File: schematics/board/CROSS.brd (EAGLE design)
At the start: 82 x 82 mm, 8 parts

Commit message: Папка с платами
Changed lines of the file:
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@@
 <setting verticaltext="up"/>
 </settings>
-<grid distance="0.5" unitdist="mm" unit="mm" style="lines" multiple="1" display="yes" altdistance="0.1" altunitdist="mm" altunit="mm"/>
+<grid distance="1" unitdist="mm" unit="mm" style="lines" multiple="1" display="no" altdistance="0.01" altunitdist="mm" altunit="mm"/>
 <layers>
 <layer number="1" name="Top" color="4" fill="1" visible="yes" active="yes"/>
@@
 <layer number="43" name="vRestrict" color="2" fill="10" visible="no" active="yes"/>
 <layer number="44" name="Drills" color="7" fill="1" visible="no" active="yes"/>
-<layer number="45" name="Holes" color="7" fill="1" visible="no" active="yes"/>
+<layer number="45" name="Holes" color="7" fill="1" visible="yes" active="yes"/>
 <layer number="46" name="Milling" color="3" fill="1" visible="no" active="yes"/>
 <layer number="47" name="Measures" color="7" fill="1" visible="no" active="yes"/>
@@
 <wire x1="34.26748125" y1="24.306490625" x2="28.8618" y2="23.204940625" width="0.1" layer="20" curve="66.964296"/>
 <wire x1="23.205" y1="28.862" x2="24.306490625" y2="34.26748125" width="0.1" layer="20" curve="66.964381"/>
-<hole x="4" y="4" drill="6"/>
-<hole x="78" y="78" drill="6"/>
-<hole x="4" y="78" drill="6"/>
-<hole x="78" y="4" drill="6"/>
+<hole x="4" y="4" drill="3.5"/>
+<hole x="78" y="78" drill="3.5"/>
+<hole x="4" y="78" drill="3.5"/>
+<hole x="78" y="4" drill="3.5"/>
 </plain>
 <attributes>

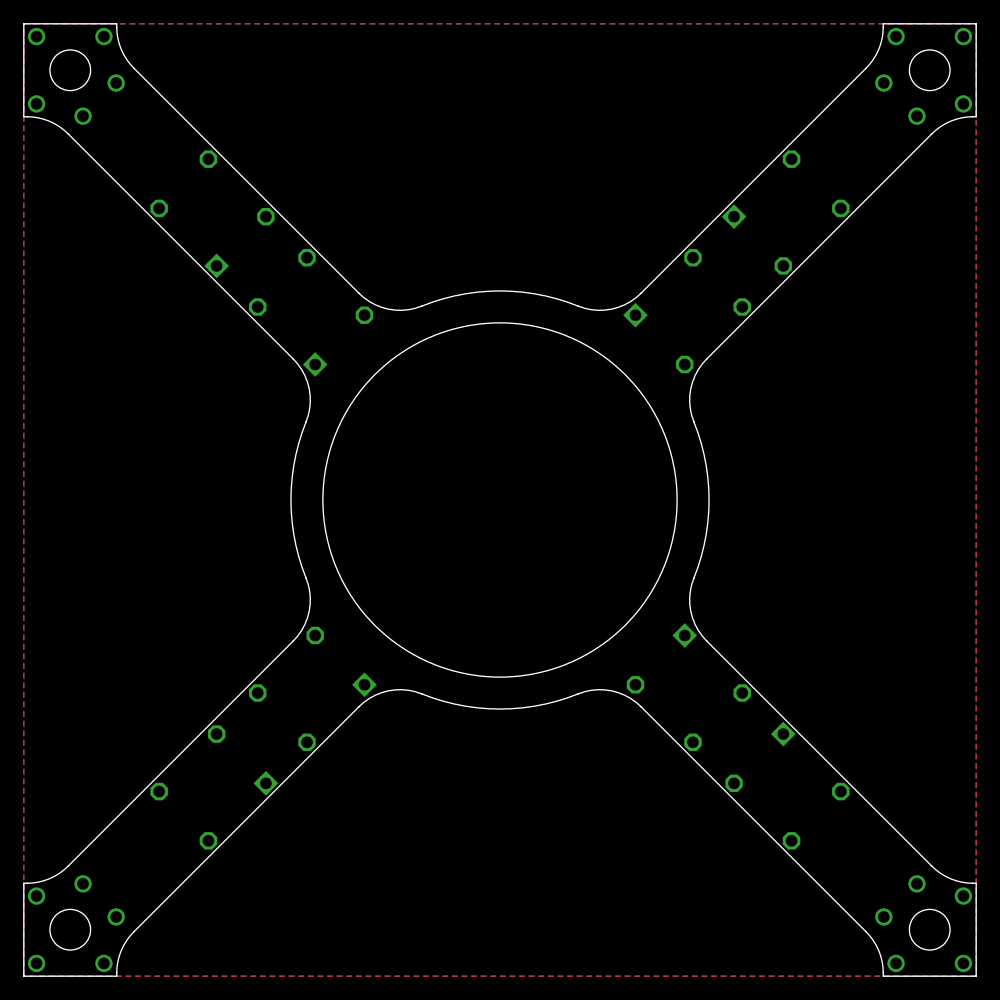
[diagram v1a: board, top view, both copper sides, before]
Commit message: Обновлен список плат, работа над платой ПН
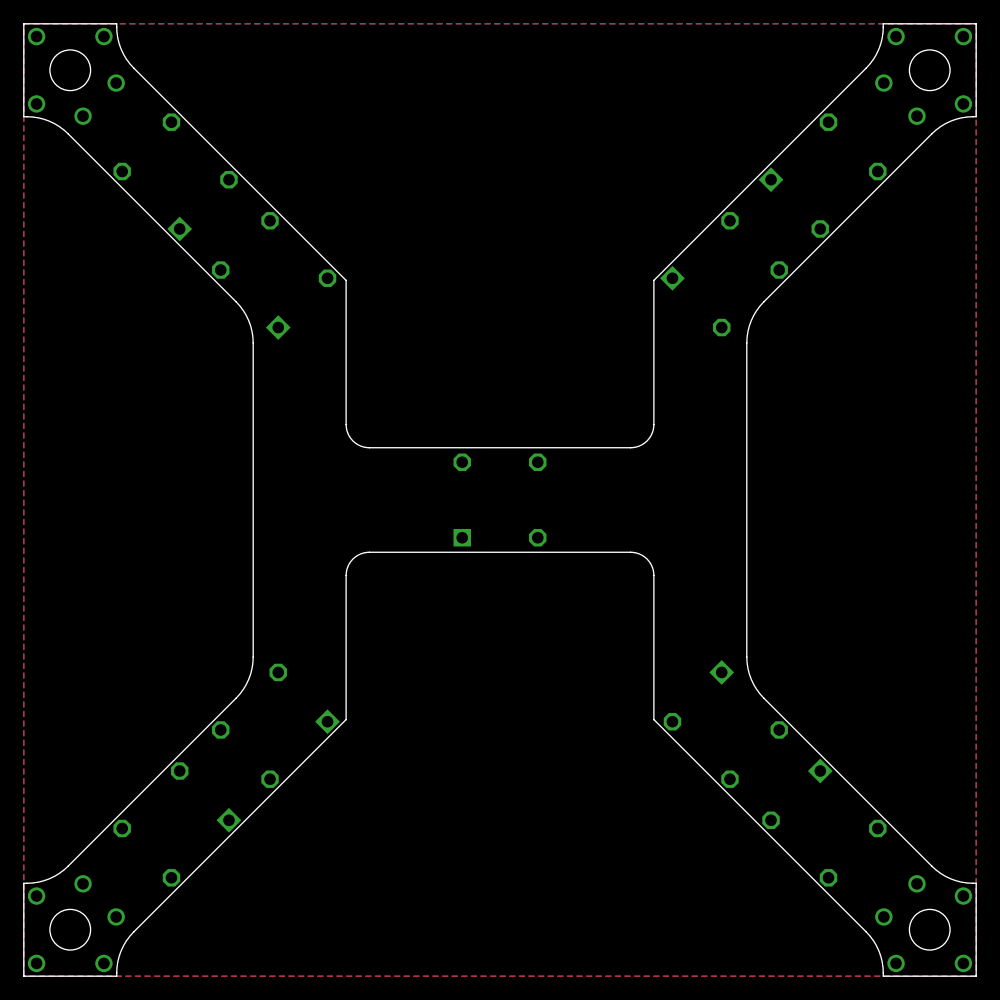
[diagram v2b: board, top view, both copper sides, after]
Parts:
- added U$5: KCONNECTQUAD-, CanCubeSat:KCONNECT-_QUAD
- moved U$3 4.50 mm to (68.9, 68.9)
- moved U$4 4.50 mm to (60.4, 60.4)
- moved U$1 4.50 mm to (13.1, 68.9)
- moved U$20 4.50 mm to (68.9, 13.1)
- moved U$18 4.50 mm to (13.1, 13.1)
- moved U$2 4.50 mm to (21.6, 60.4)
- moved U$21 4.50 mm to (60.4, 21.6)
- moved U$19 4.50 mm to (21.6, 21.6)
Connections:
- new net CMD: U$5.1, U$5.2, U$5.3, U$5.4
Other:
- outline, holes or cut-outs redrawn
